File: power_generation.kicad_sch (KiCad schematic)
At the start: 34 parts, among them J301 61300211121, J302 61300211121, J303 EMI shield frame, J304 EMI shield frame, U301 AP64500SP-13, U302 AP64500SP-13

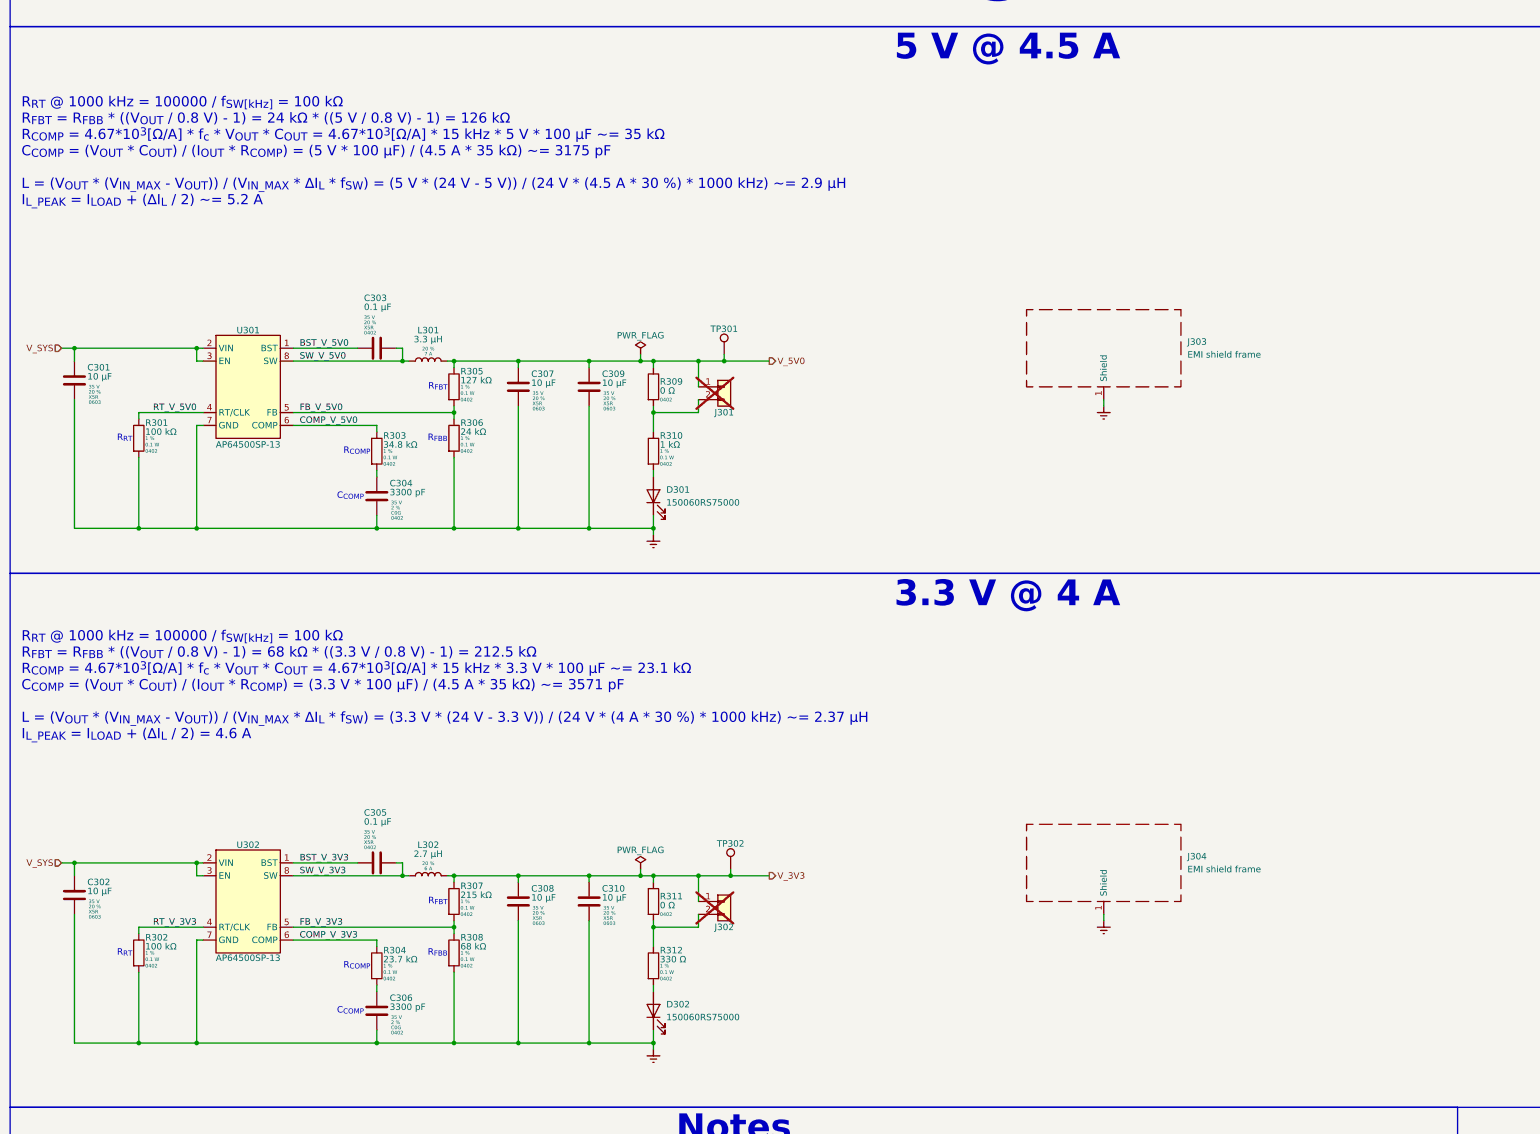
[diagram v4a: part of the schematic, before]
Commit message: Switching freq is 2 MHz, update EMI filter
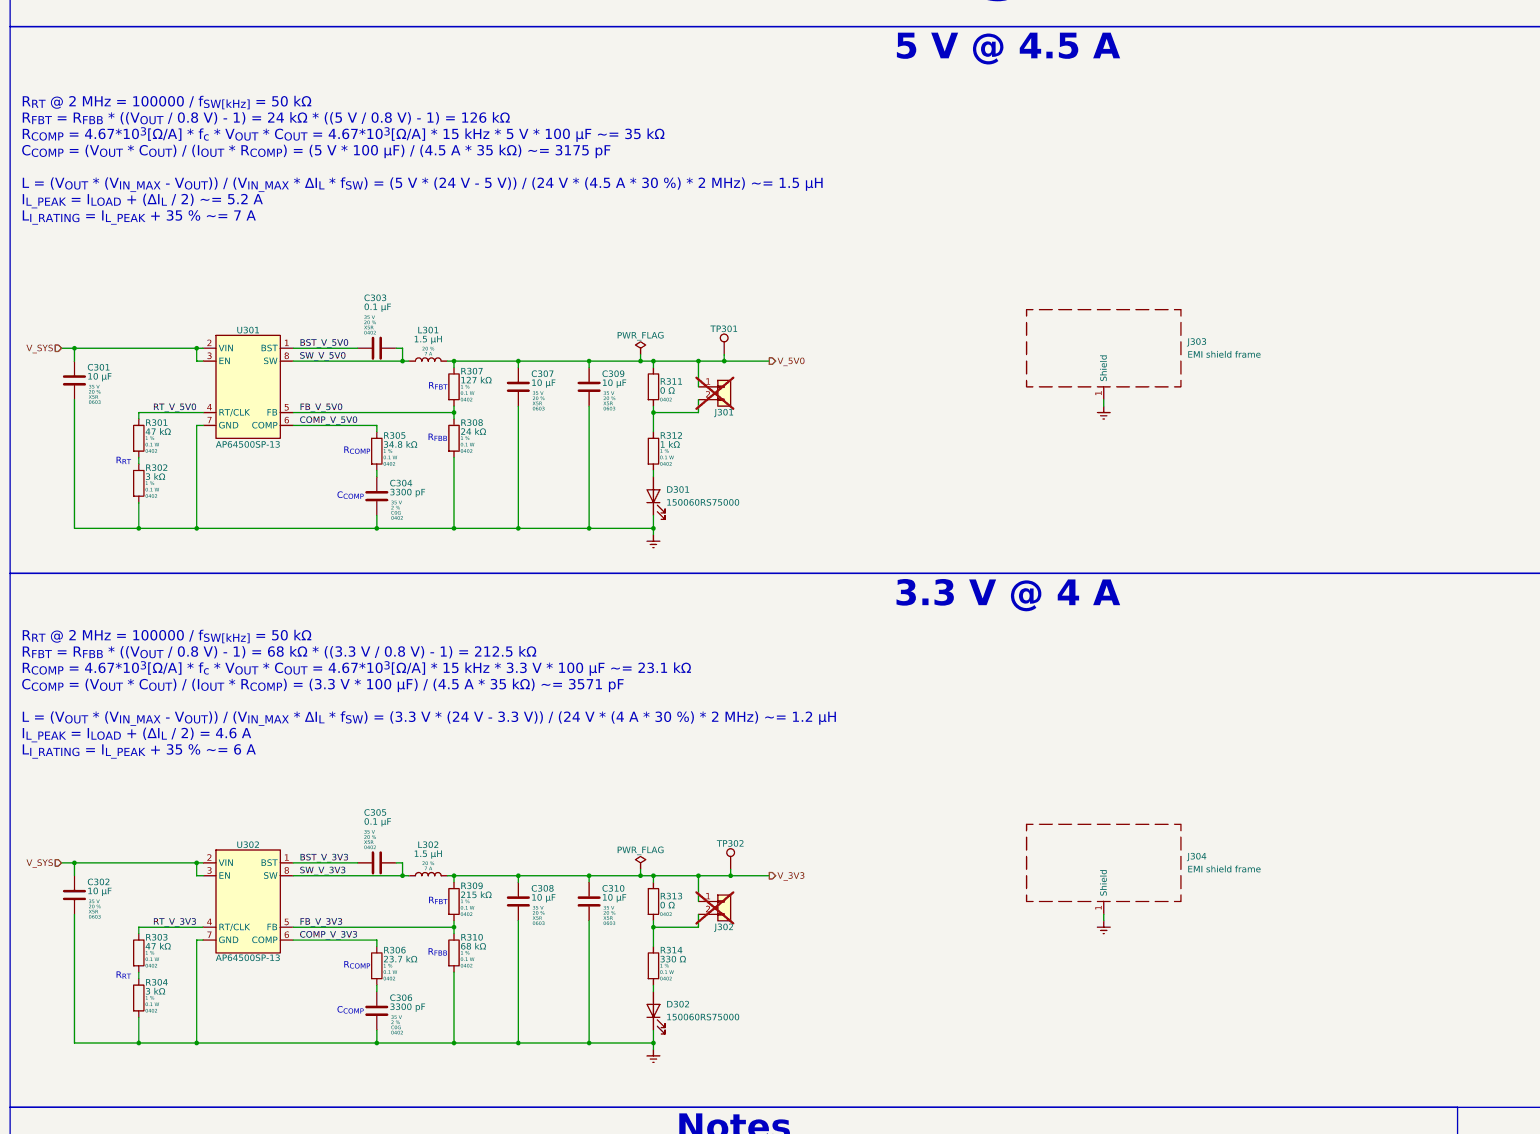
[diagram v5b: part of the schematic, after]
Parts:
- added R303: 47 kΩ, perfect_footprints:R_0402_1005Metric, symbol Device:R
- added R304: 3 kΩ, perfect_footprints:R_0402_1005Metric, symbol Device:R
- L301: value 3.3 µH -> 1.5 µH; footprint Inductor_SMD:L_Chilisin_BMRx00060630 -> Inductor_SMD:L_Vishay_IHLP-2525; Digi-Key Part Number 3526-AIP0630GX-3R3MPBDGCT-ND -> 541-1007-1-ND; MPN AIP0630GX-3R3MPBDG -> IHLP2525CZER1R5M01; Manufacturer INPAQ Technology Co., Ltd -> Vishay Dale
- L302: value 2.7 µH -> 1.5 µH; footprint Inductor_SMD:L_Bourns-SRN8040_8x8.15mm -> Inductor_SMD:L_Vishay_IHLP-2525; Current rating 6 A -> 7 A; Digi-Key Part Number 118-SRN8040HA-2R7MCT-ND -> 541-1007-1-ND; MPN SRN8040HA-2R7M -> IHLP2525CZER1R5M01; Manufacturer Bourns Inc. -> Vishay Dale
- R301: value 100 kΩ -> 47 kΩ; Digi-Key Part Number P100KLCT-ND -> P47.0KLCT-ND; MPN ERJ-2RKF1003X -> ERJ-2RKF4702X
- R302: value 100 kΩ -> 3 kΩ; Digi-Key Part Number P100KLCT-ND -> 738-RNCF0402DTE3K00CT-ND; MPN ERJ-2RKF1003X -> RNCF0402DTE3K00; Manufacturer Panasonic Electronic Components -> Stackpole Electronics Inc
- renumbered R303 to R305, R304 to R306, R305 to R307, R306 to R308, R307 to R309, R308 to R310, R309 to R311, R310 to R312, R311 to R313, R312 to R314
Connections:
- net GND: now also R304.2; no longer R301.2
- net RT_V_3V3: now also R303.1; no longer R302.1
- new net: R301.2, R302.1
- new net: R303.2, R304.1

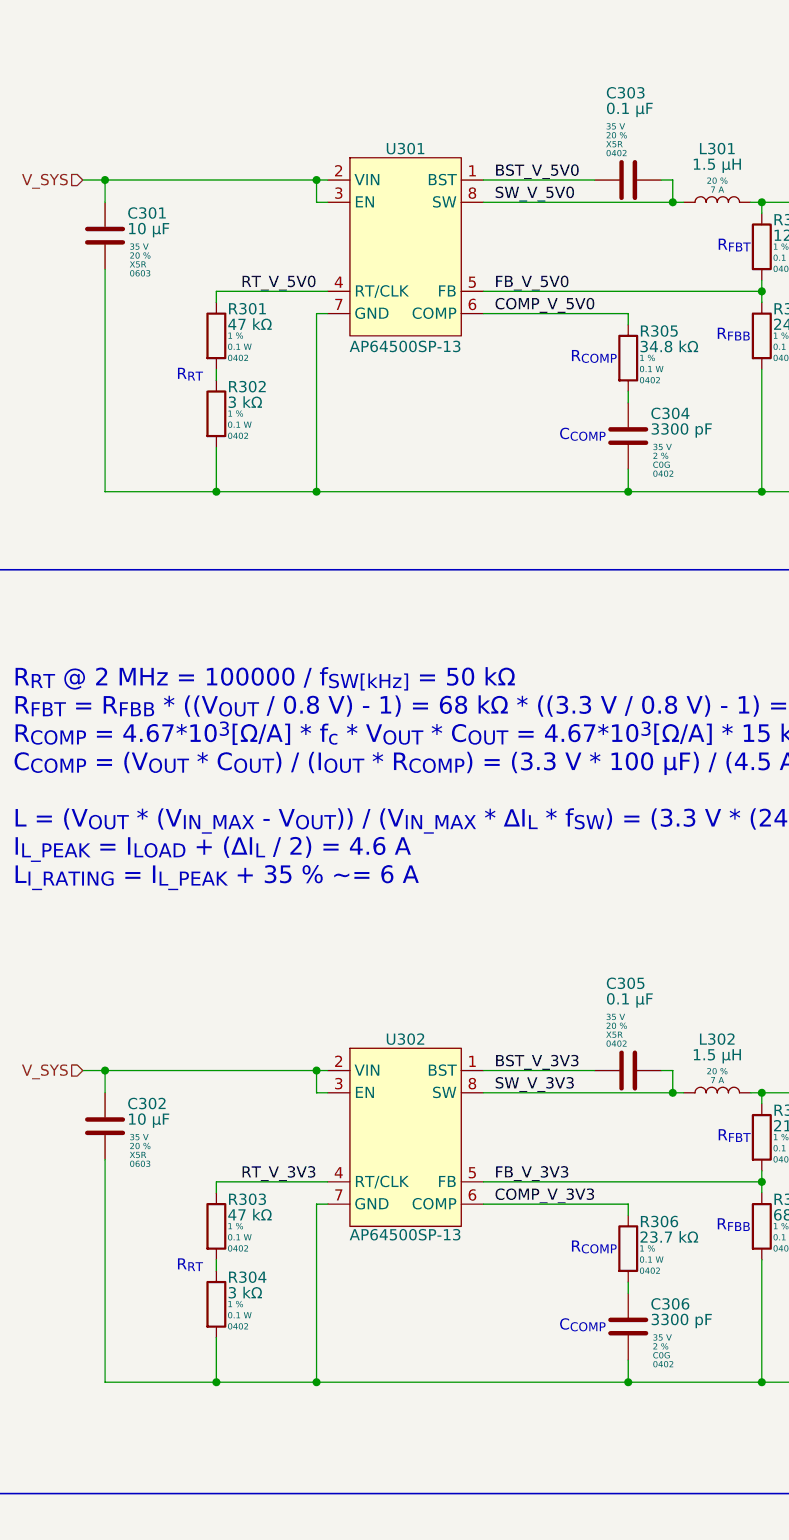
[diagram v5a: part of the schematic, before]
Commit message: Fix BOM and symbols
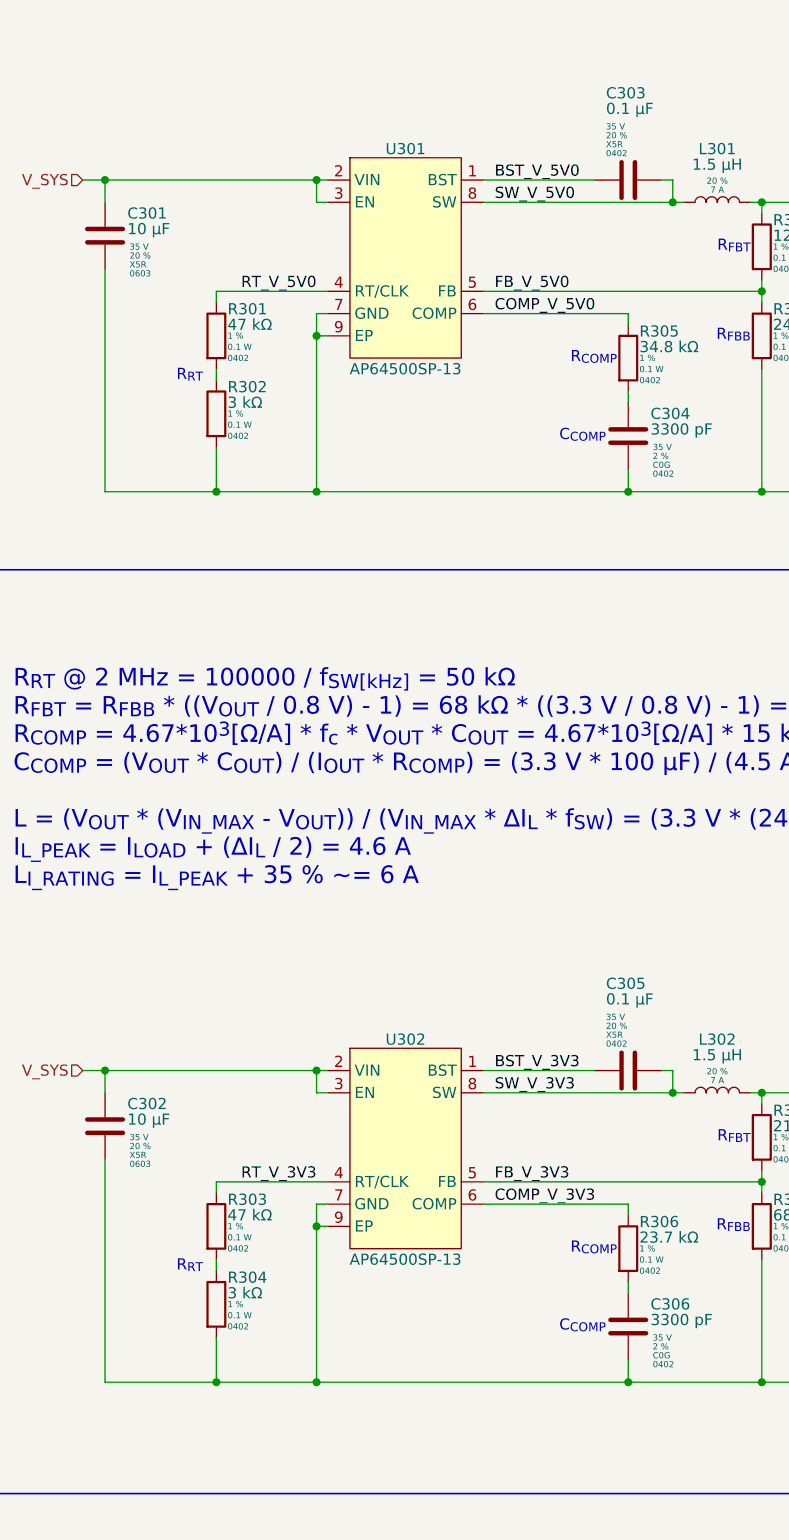
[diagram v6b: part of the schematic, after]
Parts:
- U301, U302: symbol Diodes Incorporated:AP64500 -> Diodes Incorporated:AP64500SP-13
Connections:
- net GND: now also U301.9 (EP), U302.9 (EP)
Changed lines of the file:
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@@
 	)
 	(junction
+		(at 49.53 220.98)
+		(diameter 0)
+		(color 0 0 0 0)
+	)
+	(junction
 		(at 113.03 238.76)
 		(diameter 0)
@@
 	)
 	(junction
+		(at 49.53 119.38)
+		(diameter 0)
+		(color 0 0 0 0)
+	)
+	(junction
 		(at 137.16 205.74)
 		(diameter 0)
@@
 	(wire
 		(pts
-			(xy 49.53 116.84) (xy 49.53 137.16)
+			(xy 49.53 116.84) (xy 49.53 119.38)
 		)
 		(stroke
@@
 	(wire
 		(pts
-			(xy 49.53 218.44) (xy 49.53 238.76)
+			(xy 49.53 218.44) (xy 49.53 220.98)
 		)
 		(stroke
@@
 	(wire
 		(pts
+			(xy 49.53 119.38) (xy 50.8 119.38)
+		)
+		(stroke
+			(width 0)
+			(type default)
+		)
+	)
+	(wire
+		(pts
 			(xy 68.58 116.84) (xy 85.09 116.84)
 		)
@@
 	(wire
 		(pts
+			(xy 49.53 220.98) (xy 50.8 220.98)
+		)
+		(stroke
+			(width 0)
+			(type default)
+		)
+	)
+	(wire
+		(pts
 			(xy 148.59 104.14) (xy 153.67 104.14)
 		)
@@
 	(wire
 		(pts
+			(xy 49.53 220.98) (xy 49.53 238.76)
+		)
+		(stroke
+			(width 0)
+			(type default)
+		)
+	)
+	(wire
+		(pts
 			(xy 25.4 101.6) (xy 49.53 101.6)
 		)
@@
 	(wire
 		(pts
+			(xy 49.53 119.38) (xy 49.53 137.16)
+		)
+		(stroke
+			(width 0)
+			(type default)
+		)
+	)
+	(wire
+		(pts
 			(xy 49.53 203.2) (xy 50.8 203.2)
 		)
@@
 	)
 	(symbol
-		(lib_id "Diodes Incorporated:AP64500")
+		(lib_id "Diodes Incorporated:AP64500SP-13")
 		(at 59.69 210.82 0)
 		(unit 1)
@@
 		)
 		(property "Value" "AP64500SP-13"
-			(at 59.69 221.234 0)
+			(at 59.69 224.028 0)
 			(effects
 				(font
@@
 		)
 		(property "Footprint" "Package_SO:Diodes_SO-8EP"
-			(at 59.69 221.234 0)
+			(at 59.69 223.774 0)
 			(effects
 				(font
@@
 		)
 		(property "Datasheet" "https://www.diodes.com/assets/Datasheets/AP64500.pdf"
-			(at 59.69 221.234 0)
+			(at 59.69 223.774 0)
 			(effects
 				(font
@@
 		)
 		(property "Description" "3.8V TO 40V INPUT, 5A LOW IQ SYNCHRONOUS BUCK WITH PROGRAMMABLE FREQUENCY"
-			(at 59.69 221.234 0)
+			(at 59.69 223.774 0)
 			(effects
 				(font
@@
 		)
 		(property "Digi-Key Part Number" "31-AP64500SP-13CT-ND"
-			(at 59.69 221.234 0)
+			(at 59.69 223.774 0)
 			(effects
 				(font
@@
 		)
 		(property "Manufacturer" "Diodes Incorporated"
-			(at 59.69 221.234 0)
+			(at 59.69 223.774 0)
 			(effects
 				(font
@@
 		)
 		(property "MPN" "AP64500SP-13"
-			(at 59.69 221.234 0)
+			(at 59.69 223.774 0)
 			(effects
 				(font
@@
 		(pin "2"
 		)
+		(pin "9"
+		)
 		(instances
 			(project "linux-sbc"
@@
 	)
 	(symbol
-		(lib_name "AP64500_1")
-		(lib_id "Diodes Incorporated:AP64500")
+		(lib_id "Diodes Incorporated:AP64500SP-13")
 		(at 59.69 109.22 0)
 		(unit 1)
@@
 		)
 		(property "Value" "AP64500SP-13"
-			(at 59.69 119.888 0)
+			(at 59.69 122.428 0)
 			(effects
 				(font
@@
 		)
 		(property "Footprint" "Package_SO:Diodes_SO-8EP"
-			(at 59.69 119.634 0)
+			(at 59.69 122.174 0)
 			(effects
 				(font
@@
 		)
 		(property "Datasheet" "https://www.diodes.com/assets/Datasheets/AP64500.pdf"
-			(at 59.69 119.634 0)
+			(at 59.69 122.174 0)
 			(effects
 				(font
@@
 		)
 		(property "Description" "3.8V TO 40V INPUT, 5A LOW IQ SYNCHRONOUS BUCK WITH PROGRAMMABLE FREQUENCY"
-			(at 59.69 119.634 0)
+			(at 59.69 122.174 0)
 			(effects
 				(font
@@
 		)
 		(property "Digi-Key Part Number" "31-AP64500SP-13CT-ND"
-			(at 59.69 119.634 0)
+			(at 59.69 122.174 0)
 			(effects
 				(font
@@
 		)
 		(property "Manufacturer" "Diodes Incorporated"
-			(at 59.69 119.634 0)
+			(at 59.69 122.174 0)
 			(effects
 				(font
@@
 		)
 		(property "MPN" "AP64500SP-13"
-			(at 59.69 119.634 0)
+			(at 59.69 122.174 0)
 			(effects
 				(font
@@
 		(pin "2"
 		)
+		(pin "9"
+		)
 		(instances

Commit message: Connect ESD TVS to chassis where possible, update version and date
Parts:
- removed J304: EMI shield frame, RF_Shielding:Laird_Technologies_BMI-S-202-F_16.50x16.50mm, symbol Device:RFShield_OnePiece
- J303: footprint RF_Shielding:Laird_Technologies_BMI-S-202-F_16.50x16.50mm -> RF_Shielding:Laird_Technologies_BMI-S-203-F_26.21x26.21mm
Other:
- note added: "Place both inside the EMI shield frame."
- moved on the sheet: C301, C302, C303, C304, C305, C306, C307, C308, C309, C310, D301, D302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
